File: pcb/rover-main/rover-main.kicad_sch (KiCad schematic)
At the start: 0 parts

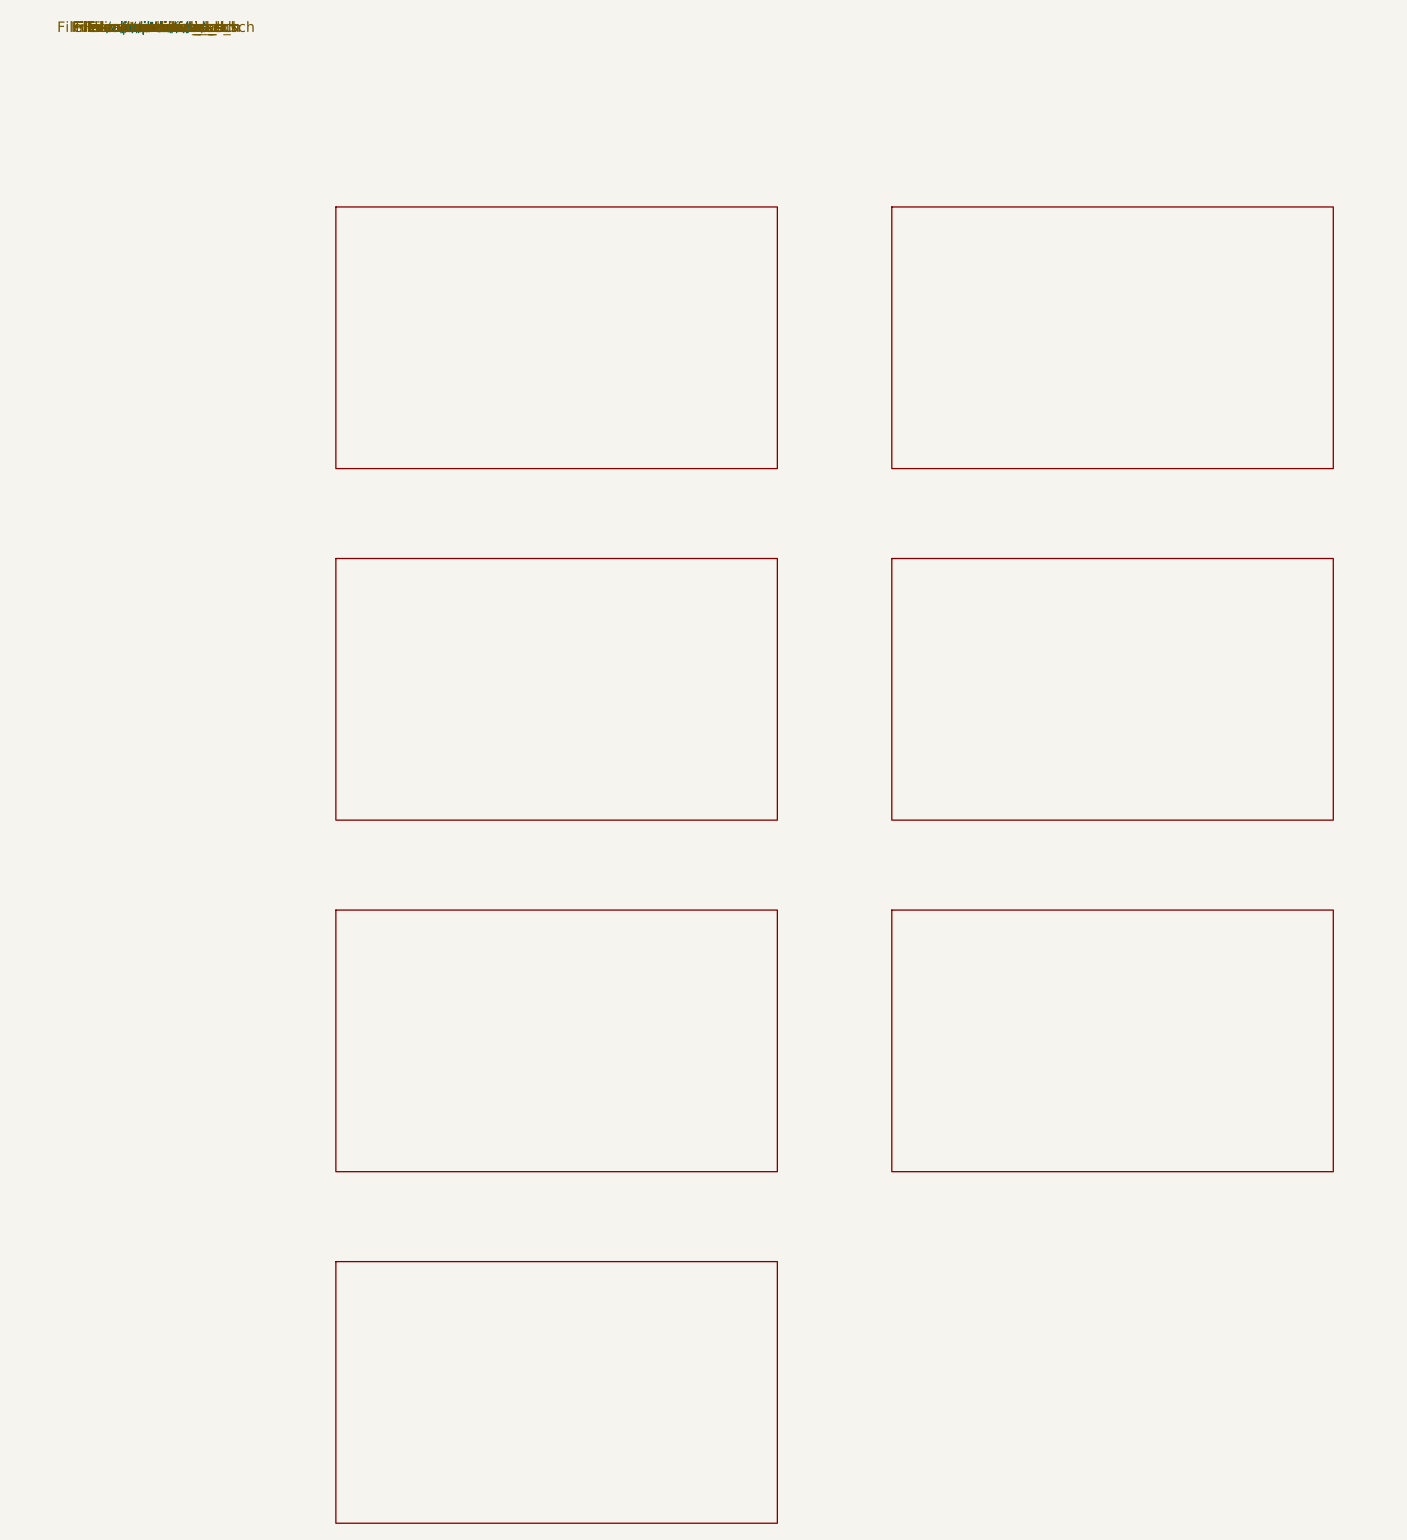
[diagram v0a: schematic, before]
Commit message: Add a more concrete KiCad schematic draft with key blocks and real net names for the Rover PCB design.
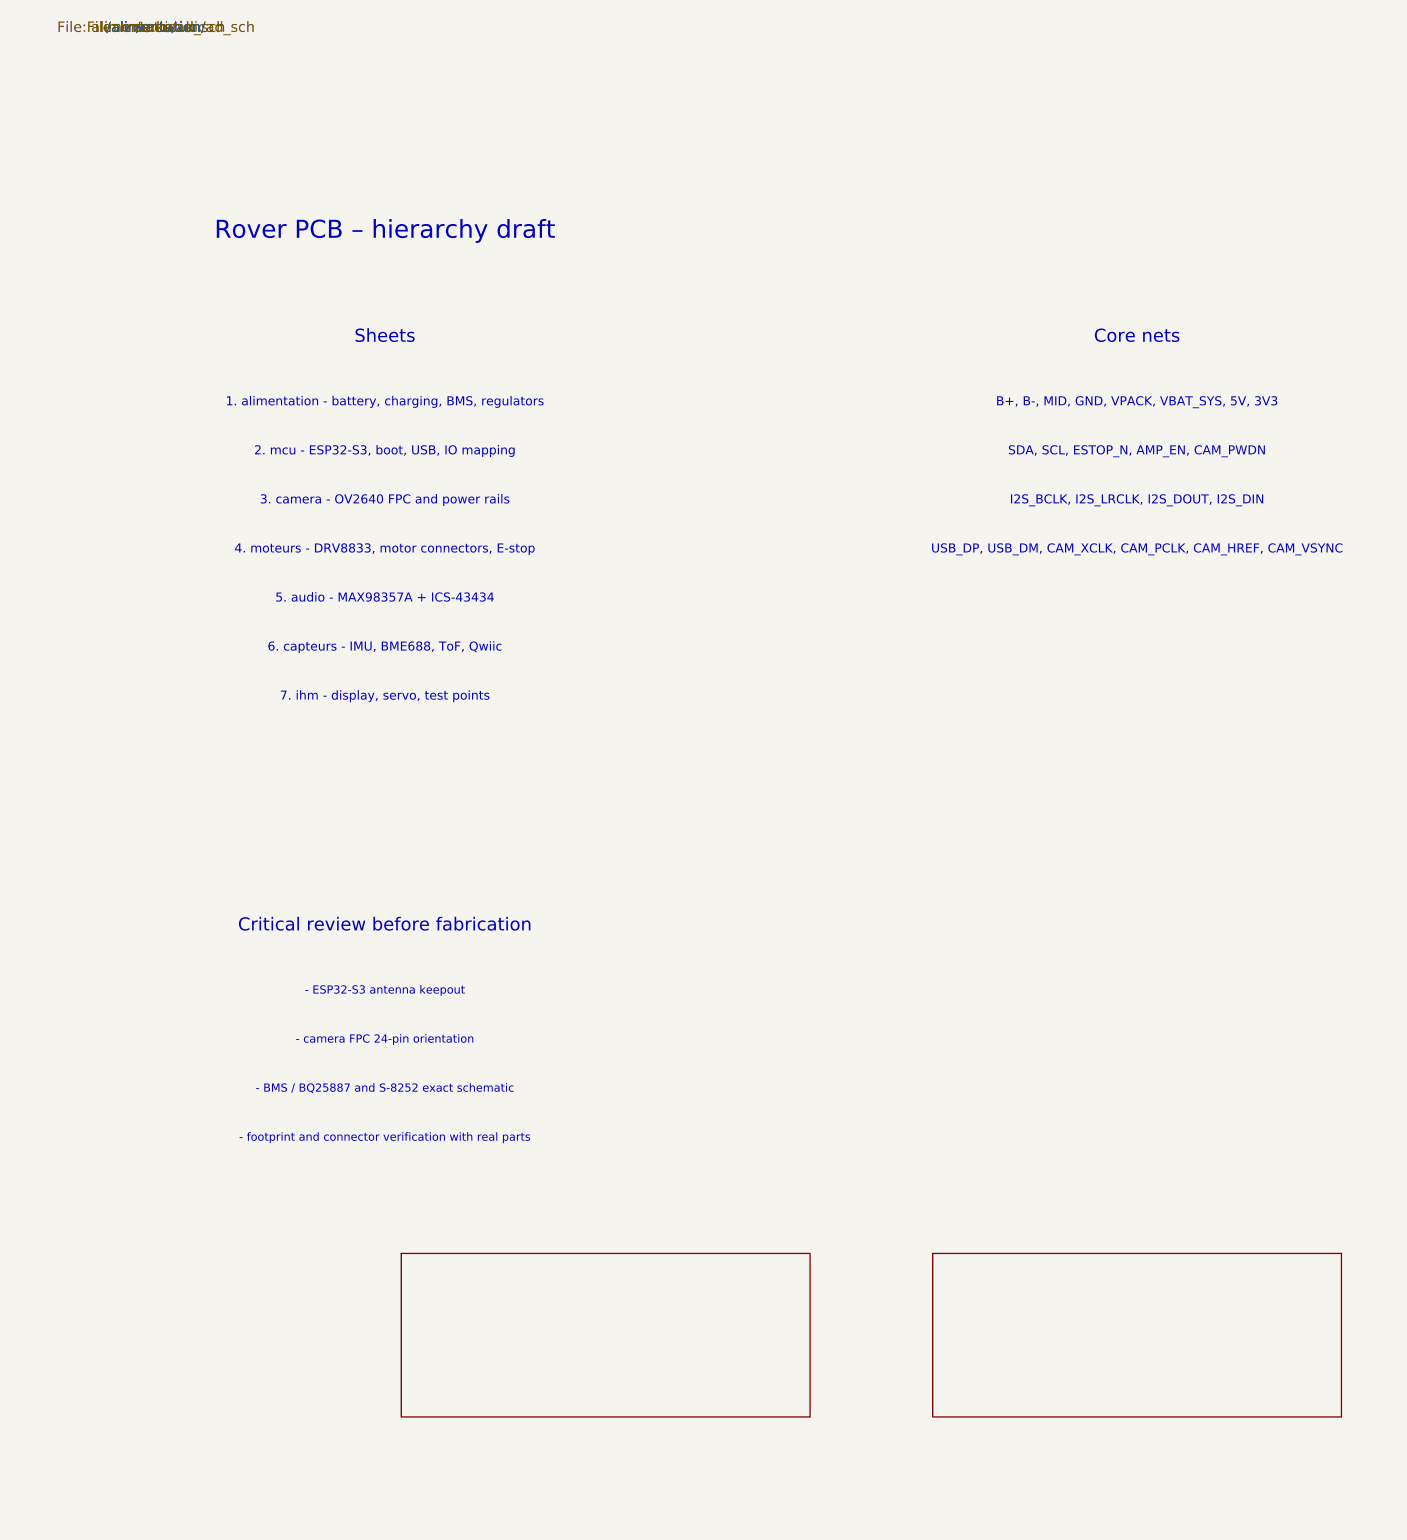
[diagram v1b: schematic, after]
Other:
- removed sheet audio
- removed sheet camera
- removed sheet capteurs
- removed sheet ihm
- removed sheet moteurs
- note added: "- BMS / BQ25887 and S-8252 exact schematic"
- note added: "- ESP32-S3 antenna keepout"
- note added: "- camera FPC 24-pin orientation"
- note added: "- footprint and connector verification with real parts"
- note added: "1. alimentation - battery, charging, BMS, regulators"
- note added: "2. mcu - ESP32-S3, boot, USB, IO mapping"
- note added: "3. camera - OV2640 FPC and power rails"
- note added: "4. moteurs - DRV8833, motor connectors, E-stop"
- note added: "5. audio - MAX98357A + ICS-43434"
- note added: "6. capteurs - IMU, BME688, ToF, Qwiic"
- note added: "7. ihm - display, servo, test points"
- note added: "B+, B-, MID, GND, VPACK, VBAT_SYS, 5V, 3V3"
- note added: "Core nets"
- note added: "Critical review before fabrication"
- note added: "I2S_BCLK, I2S_LRCLK, I2S_DOUT, I2S_DIN"
- note added: "Rover PCB – hierarchy draft"
- note added: "SDA, SCL, ESTOP_N, AMP_EN, CAM_PWDN"
- note added: "Sheets"
- note added: "USB_DP, USB_DM, CAM_XCLK, CAM_PCLK, CAM_HREF, CAM_VSYNC"
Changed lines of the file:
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@@
 (kicad_sch
-  (version 20250114)
-  (generator "KiCad")
+  (version 20211014)
+  (generator "eeschema")
   (paper "A4")
   (title_block
     (title "Rover PCB draft")
     (date "2026-10-13")
-    (rev "0.1")
+    (rev "0.2")
     (company "Rover Project")
-    (comment 1 "Draft only - not fabrication-ready")
+    (comment 1 "Draft schematic, human review required before fabrication")
+  )
+  (text "Rover PCB – hierarchy draft" (at 28 25 0)
+    (effects (font (size 2.2 2.2) (thickness 0.3)))
+  )
+  (text "Sheets" (at 28 38 0)
+    (effects (font (size 1.6 1.6) (thickness 0.22)))
+  )
+  (text "1. alimentation - battery, charging, BMS, regulators" (at 28 46 0)
+    (effects (font (size 1.1 1.1)))
+  )
+  (text "2. mcu - ESP32-S3, boot, USB, IO mapping" (at 28 52 0)
+    (effects (font (size 1.1 1.1)))
+  )
+  (text "3. camera - OV2640 FPC and power rails" (at 28 58 0)
+    (effects (font (size 1.1 1.1)))
+  )
+  (text "4. moteurs - DRV8833, motor connectors, E-stop" (at 28 64 0)
+    (effects (font (size 1.1 1.1)))
+  )
+  (text "5. audio - MAX98357A + ICS-43434" (at 28 70 0)
+    (effects (font (size 1.1 1.1)))
+  )
+  (text "6. capteurs - IMU, BME688, ToF, Qwiic" (at 28 76 0)
+    (effects (font (size 1.1 1.1)))
+  )
+  (text "7. ihm - display, servo, test points" (at 28 82 0)
+    (effects (font (size 1.1 1.1)))
+  )
+  (text "Core nets" (at 120 38 0)
+    (effects (font (size 1.6 1.6) (thickness 0.22)))
+  )
+  (text "B+, B-, MID, GND, VPACK, VBAT_SYS, 5V, 3V3" (at 120 46 0)
+    (effects (font (size 1.1 1.1)))
+  )
+  (text "SDA, SCL, ESTOP_N, AMP_EN, CAM_PWDN" (at 120 52 0)
+    (effects (font (size 1.1 1.1)))
+  )
+  (text "I2S_BCLK, I2S_LRCLK, I2S_DOUT, I2S_DIN" (at 120 58 0)
+    (effects (font (size 1.1 1.1)))
+  )
+  (text "USB_DP, USB_DM, CAM_XCLK, CAM_PCLK, CAM_HREF, CAM_VSYNC" (at 120 64 0)
+    (effects (font (size 1.1 1.1)))
+  )
+  (text "Critical review before fabrication" (at 28 110 0)
+    (effects (font (size 1.6 1.6) (thickness 0.22)))
+  )
+  (text "- ESP32-S3 antenna keepout" (at 28 118 0)
+    (effects (font (size 1.0 1.0)))
+  )
+  (text "- camera FPC 24-pin orientation" (at 28 124 0)
+    (effects (font (size 1.0 1.0)))
+  )
+  (text "- BMS / BQ25887 and S-8252 exact schematic" (at 28 130 0)
+    (effects (font (size 1.0 1.0)))
+  )
+  (text "- footprint and connector verification with real parts" (at 28 136 0)
+    (effects (font (size 1.0 1.0)))
   )
   (sheet
-    (at 22 22)
-    (size 54 32)
+    (at 30 150)
+    (size 50 20)
     (stroke (width 0.1) (type solid))
     (fill (color 0 0 0 0.0000))
-    (text "alimentation" (at 49 39 0)
-      (effects (font (size 2.5 2.5) (thickness 0.3)))
-    )
-    (text "battery, protection, charge, buck" (at 38 31 0)
-      (effects (font (size 1.0 1.0)))
+    (text "alimentation" (at 55 163 0)
+      (effects (font (size 2.0 2.0) (thickness 0.2)))
     )
     (property "Sheetname" "alimentation")
@@
   )
   (sheet
-    (at 90 22)
-    (size 54 32)
+    (at 95 150)
+    (size 50 20)
     (stroke (width 0.1) (type solid))
     (fill (color 0 0 0 0.0000))
-    (text "mcu" (at 117 39 0)
-      (effects (font (size 2.5 2.5) (thickness 0.3)))
-    )
-    (text "ESP32-S3 + USB + IO + TCA9554" (at 97 31 0)
-      (effects (font (size 1.0 1.0)))
+    (text "mcu" (at 120 163 0)
+      (effects (font (size 2.0 2.0) (thickness 0.2)))
     )
     (property "Sheetname" "mcu")
@@
     (property "Sheetpath" "/mcu/")
   )
-  (sheet
-    (at 22 65)
-    (size 54 32)
-    (stroke (width 0.1) (type solid))
-    (fill (color 0 0 0 0.0000))
-    (text "camera" (at 49 82 0)
-      (effects (font (size 2.5 2.5) (thickness 0.3)))
-    )
-    (text "OV2640 + SCCB + supplies" (at 38 74 0)
-      (effects (font (size 1.0 1.0)))
-    )
-    (property "Sheetname" "camera")
-    (property "Sheetfile" "camera.kicad_sch")
-    (property "Sheetpath" "/camera/")
-  )
-  (sheet
-    (at 90 65)
-    (size 54 32)
-    (stroke (width 0.1) (type solid))
-    (fill (color 0 0 0 0.0000))
-    (text "moteurs" (at 117 82 0)
-      (effects (font (size 2.5 2.5) (thickness 0.3)))
-    )
-    (text "DRV8833 + E-stop + motor connectors" (at 98 74 0)
-      (effects (font (size 1.0 1.0)))
-    )
-    (property "Sheetname" "moteurs")
-    (property "Sheetfile" "moteurs.kicad_sch")
-    (property "Sheetpath" "/moteurs/")
-  )
-  (sheet
-    (at 22 108)
-    (size 54 32)
-    (stroke (width 0.1) (type solid))
-    (fill (color 0 0 0 0.0000))
-    (text "audio" (at 49 125 0)
-      (effects (font (size 2.5 2.5) (thickness 0.3)))
-    )
-    (text "MAX98357A + ICS-43434 + I2S" (at 42 117 0)
-      (effects (font (size 1.0 1.0)))
-    )
-    (property "Sheetname" "audio")
-    (property "Sheetfile" "audio.kicad_sch")
-    (property "Sheetpath" "/audio/")
-  )
-  (sheet
-    (at 90 108)
-    (size 54 32)
-    (stroke (width 0.1) (type solid))
-    (fill (color 0 0 0 0.0000))
-    (text "capteurs" (at 117 125 0)
-      (effects (font (size 2.5 2.5) (thickness 0.3)))
-    )
-    (text "IMU + BME688 + ToF + Qwiic" (at 101 117 0)
-      (effects (font (size 1.0 1.0)))
-    )
-    (property "Sheetname" "capteurs")
-    (property "Sheetfile" "capteurs.kicad_sch")
-    (property "Sheetpath" "/capteurs/")
-  )
-  (sheet
-    (at 22 151)
-    (size 54 32)
-    (stroke (width 0.1) (type solid))
-    (fill (color 0 0 0 0.0000))
-    (text "ihm" (at 49 168 0)
-      (effects (font (size 2.5 2.5) (thickness 0.3)))
-    )
-    (text "display + servo + LED + test points" (at 38 160 0)
-      (effects (font (size 1.0 1.0)))
-    )
-    (property "Sheetname" "ihm")
-    (property "Sheetfile" "ihm.kicad_sch")
-    (property "Sheetpath" "/ihm/")
-  )
-  (sheet_instances
-    (path "/alimentation" (page "1"))
-    (path "/mcu" (page "1"))
-    (path "/camera" (page "1"))
-    (path "/moteurs" (page "1"))
-    (path "/audio" (page "1"))
-    (path "/capteurs" (page "1"))
-    (path "/ihm" (page "1"))
-  )
 )
